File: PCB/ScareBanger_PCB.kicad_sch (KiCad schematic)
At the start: 25 parts, among them J1 RJ45, J16 Conn_01x10_Female - SAINSMART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, J17 Screw_Terminal_01x10 - HILETG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, J2 1757271, J3 Screw_Terminal_01x06, J4 Barrel_Jack_Switch, J5 AudioJack2_Ground, J6 Screw_Terminal_01x06, J7 Screw_Terminal_01x06, J8 Conn_01x04_Female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

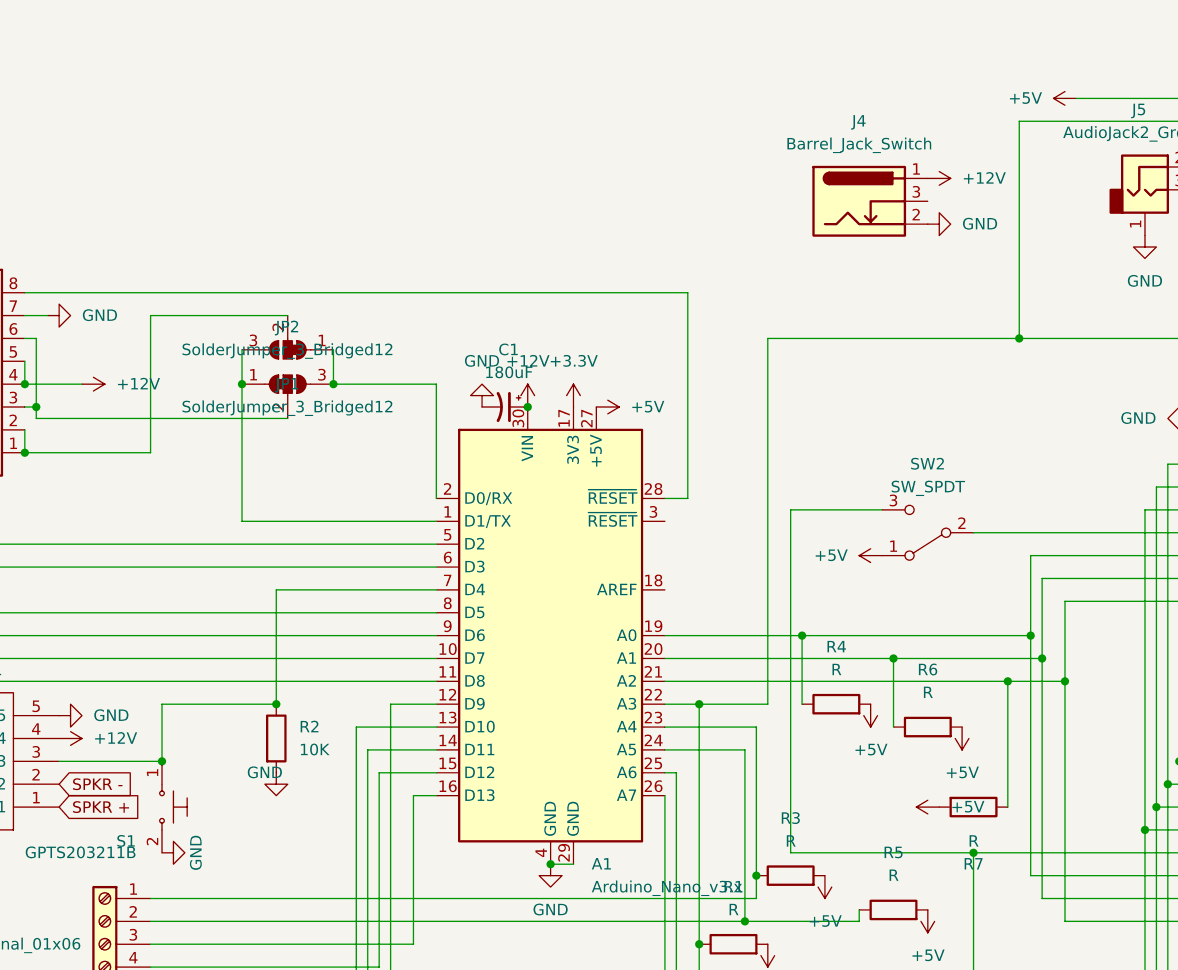
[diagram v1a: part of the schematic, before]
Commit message: added signal cap
added capacitor for signal wire, and  changed the main 12v trace to be 2mm wide
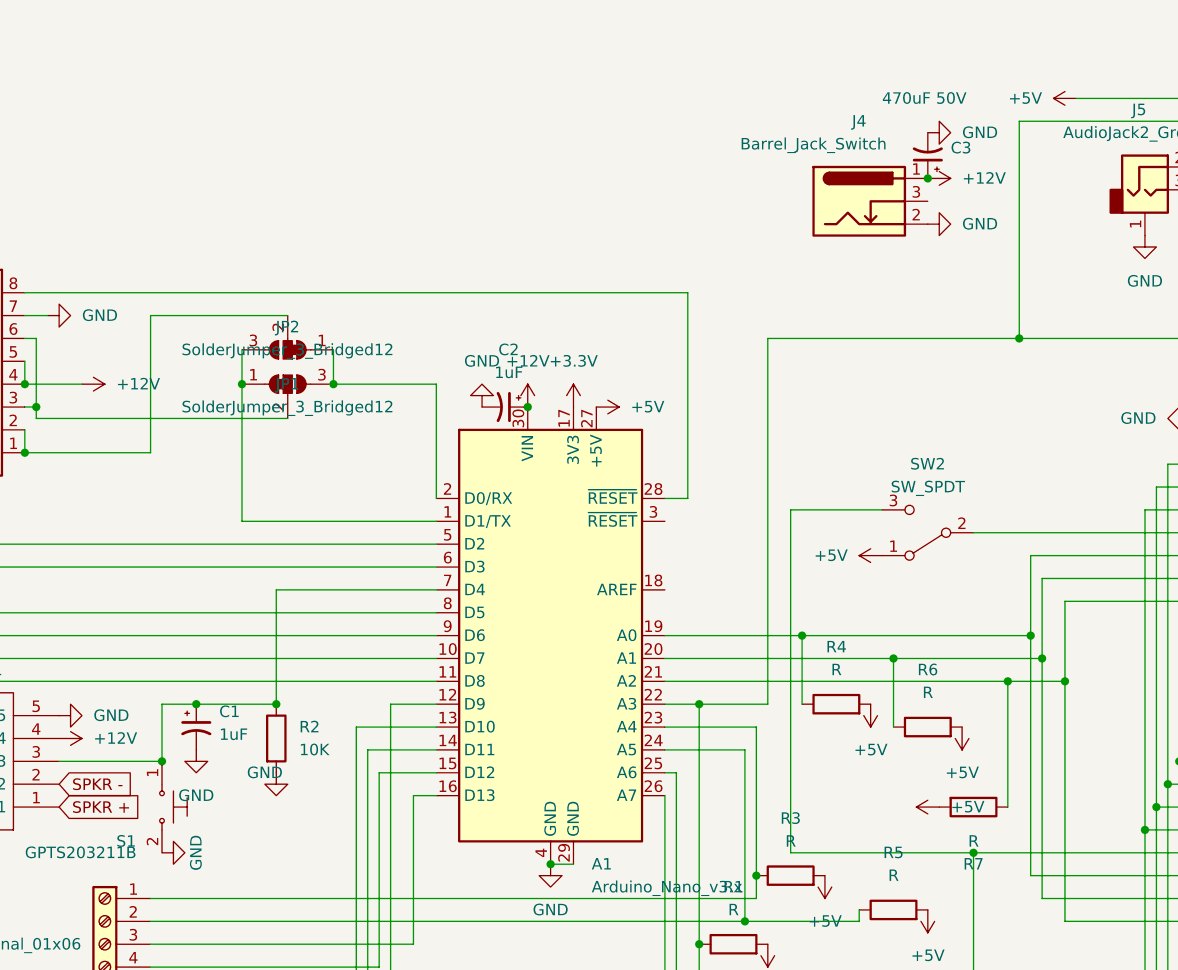
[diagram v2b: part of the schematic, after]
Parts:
- added C2: 1uF, Capacitor_THT:CP_Radial_D4.0mm_P1.50mm, symbol Device:C_Polarized_Small_US
- added C3: 470uF 50V, Capacitor_THT:CP_Radial_D8.0mm_P3.50mm, symbol Device:C_Polarized_Small_US
- C1: value 180uF -> 1uF; footprint Capacitor_THT:CP_Radial_D6.3mm_P2.50mm -> Capacitor_THT:CP_Radial_D4.0mm_P1.50mm
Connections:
- net +12V: now also C2.1, C3.1; no longer C1.1
- net GND: now also C2.2, C3.2
- net at A1.7 (D4), J2.3, R2.1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: now also C1.1
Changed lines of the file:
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@@
   (junction (at 45.72 60.96) (diameter 0) (color 0 0 0 0)
   )
+  (junction (at 144.78 35.56) (diameter 0) (color 0 0 0 0)
+  )
   (junction (at 140.97 88.9) (diameter 0) (color 0 0 0 0)
   )
@@
   (junction (at 168.91 107.95) (diameter 0) (color 0 0 0 0)
   )
+  (junction (at 59.69 100.33) (diameter 0) (color 0 0 0 0)
+  )
+  (junction (at 68.58 58.42) (diameter 0) (color 0 0 0 0)
+  )
+  (junction (at 44.45 58.42) (diameter 0) (color 0 0 0 0)
+  )
+  (junction (at 72.39 93.98) (diameter 0) (color 0 0 0 0)
+  )
+  (junction (at 160.02 91.44) (diameter 0) (color 0 0 0 0)
+  )
+  (junction (at 63.5 93.98) (diameter 0) (color 0 0 0 0)
+  )
+  (junction (at 119.38 93.98) (diameter 0) (color 0 0 0 0)
+  )
+  (junction (at 157.48 88.9) (diameter 0) (color 0 0 0 0)
+  )
+  (junction (at 78.74 58.42) (diameter 0) (color 0 0 0 0)
+  )
+  (junction (at 154.94 53.34) (diameter 0) (color 0 0 0 0)
+  )
+  (junction (at 119.38 120.65) (diameter 0) (color 0 0 0 0)
+  )
+  (junction (at 172.72 100.33) (diameter 0) (color 0 0 0 0)
+  )
   (junction (at 100.33 60.96) (diameter 0) (color 0 0 0 0)
   )
-  (junction (at 59.69 100.33) (diameter 0) (color 0 0 0 0)
-  )
-  (junction (at 68.58 58.42) (diameter 0) (color 0 0 0 0)
-  )
-  (junction (at 44.45 58.42) (diameter 0) (color 0 0 0 0)
-  )
-  (junction (at 72.39 93.98) (diameter 0) (color 0 0 0 0)
-  )
-  (junction (at 160.02 91.44) (diameter 0) (color 0 0 0 0)
-  )
-  (junction (at 119.38 93.98) (diameter 0) (color 0 0 0 0)
-  )
-  (junction (at 157.48 88.9) (diameter 0) (color 0 0 0 0)
-  )
-  (junction (at 78.74 58.42) (diameter 0) (color 0 0 0 0)
-  )
-  (junction (at 154.94 53.34) (diameter 0) (color 0 0 0 0)
-  )
-  (junction (at 119.38 120.65) (diameter 0) (color 0 0 0 0)
-  )
-  (junction (at 172.72 100.33) (diameter 0) (color 0 0 0 0)
-  )
   (junction (at 156.21 86.36) (diameter 0) (color 0 0 0 0)
   )
@@
     (stroke (width 0) (type default) (color 0 0 0 0))
   )
+  (wire (pts (xy 59.69 93.98) (xy 63.5 93.98))
+    (stroke (width 0) (type default) (color 0 0 0 0))
+  )
   (wire (pts (xy 31.75 129.54) (xy 168.91 129.54))
     (stroke (width 0) (type default) (color 0 0 0 0))
@@
     (stroke (width 0) (type default) (color 0 0 0 0))
   )
+  (wire (pts (xy 63.5 93.98) (xy 72.39 93.98))
+    (stroke (width 0) (type default) (color 0 0 0 0))
+  )
   (wire (pts (xy 116.84 101.6) (xy 116.84 140.97))
     (stroke (width 0) (type default) (color 0 0 0 0))
@@
   )
   (wire (pts (xy 83.82 101.6) (xy 90.17 101.6))
-    (stroke (width 0) (type default) (color 0 0 0 0))
-  )
-  (wire (pts (xy 59.69 93.98) (xy 72.39 93.98))
     (stroke (width 0) (type default) (color 0 0 0 0))
   )
@@
     (pin "1")
   )
+  (symbol (lib_id "Device:C_Polarized_Small_US") (at 63.5 96.52 0) (unit 1)
+    (in_bom yes) (on_board yes) (fields_autoplaced)
+    (property "Reference" "C1" (id 0) (at 66.04 94.8181 0)
+      (effects (font (size 1.27 1.27)) (justify left))
+    )
+    (property "Value" "1uF" (id 1) (at 66.04 97.3581 0)
+      (effects (font (size 1.27 1.27)) (justify left))
+    )
+    (property "Footprint" "Capacitor_THT:CP_Radial_D4.0mm_P1.50mm" (id 2) (at 63.5 96.52 0)
+      (effects (font (size 1.27 1.27)) hide)
+    )
+    (property "Datasheet" "~" (id 3) (at 63.5 96.52 0)
+      (effects (font (size 1.27 1.27)) hide)
+    )
+    (pin "1")
+    (pin "2")
+  )
   (symbol (lib_id "power:+3.3V") (at 116.84 173.99 270) (unit 1)
     (in_bom yes) (on_board yes) (fields_autoplaced)
@@
     (pin "1")
   )
+  (symbol (lib_id "power:GND") (at 144.78 30.48 90) (unit 1)
+    (in_bom yes) (on_board yes) (fields_autoplaced)
+    (property "Reference" "#PWR0139" (id 0) (at 151.13 30.48 0)
+      (effects (font (size 1.27 1.27)) hide)
+    )
+    (property "Value" "GND" (id 1) (at 148.59 30.4799 90)
+      (effects (font (size 1.27 1.27)) (justify right))
+    )
+    (property "Footprint" "" (id 2) (at 144.78 30.48 0)
+      (effects (font (size 1.27 1.27)) hide)
+    )
+    (property "Datasheet" "" (id 3) (at 144.78 30.48 0)
+      (effects (font (size 1.27 1.27)) hide)
+    )
+    (pin "1")
+  )
   (symbol (lib_id "Device:R") (at 182.88 26.67 90) (unit 1)
     (in_bom yes) (on_board yes) (fields_autoplaced)
@@
   )
   (symbol (lib_id "power:+12V") (at 144.78 35.56 270) (unit 1)
-    (in_bom yes) (on_board yes) (fields_autoplaced)
+    (in_bom yes) (on_board yes)
     (property "Reference" "#PWR0110" (id 0) (at 140.97 35.56 0)
       (effects (font (size 1.27 1.27)) hide)
     )
-    (property "Value" "+12V" (id 1) (at 148.59 35.5599 90)
+    (property "Value" "+12V" (id 1) (at 148.59 35.56 90)
       (effects (font (size 1.27 1.27)) (justify left))
     )
@@
     (pin "5")
     (pin "6")
+  )
+  (symbol (lib_id "Device:C_Polarized_Small_US") (at 144.78 33.02 180) (unit 1)
+    (in_bom yes) (on_board yes)
+    (property "Reference" "C3" (id 0) (at 147.32 32.1817 0)
+      (effects (font (size 1.27 1.27)) (justify right))
+    )
+    (property "Value" "470uF 50V" (id 1) (at 139.7 26.67 0)
+      (effects (font (size 1.27 1.27)) (justify right))
+    )
+    (property "Footprint" "Capacitor_THT:CP_Radial_D8.0mm_P3.50mm" (id 2) (at 144.78 33.02 0)
+      (effects (font (size 1.27 1.27)) hide)
+    )
+    (property "Datasheet" "~" (id 3) (at 144.78 33.02 0)
+      (effects (font (size 1.27 1.27)) hide)
+    )
+    (pin "1")
+    (pin "2")
   )
   (symbol (lib_id "Connector:Screw_Terminal_01x10") (at 187.96 105.41 0) (unit 1)
@@
     (pin "1")
   )
-  (symbol (lib_id "Device:C_Polarized_Small_US") (at 97.79 60.96 270) (unit 1)
-    (in_bom yes) (on_board yes) (fields_autoplaced)
-    (property "Reference" "C1" (id 0) (at 98.2218 54.61 90))
-    (property "Value" "180uF" (id 1) (at 98.2218 57.15 90))
-    (property "Footprint" "Capacitor_THT:CP_Radial_D6.3mm_P2.50mm" (id 2) (at 97.79 60.96 0)
-      (effects (font (size 1.27 1.27)) hide)
-    )
-    (property "Datasheet" "~" (id 3) (at 97.79 60.96 0)
-      (effects (font (size 1.27 1.27)) hide)
-    )
-    (pin "1")
-    (pin "2")
-  )
   (symbol (lib_id "power:GND") (at 182.88 97.79 270) (unit 1)
     (in_bom yes) (on_board yes) (fields_autoplaced)
@@
     )
     (pin "1")
+  )
+  (symbol (lib_id "Device:C_Polarized_Small_US") (at 97.79 60.96 270) (unit 1)
+    (in_bom yes) (on_board yes) (fields_autoplaced)
+    (property "Reference" "C2" (id 0) (at 98.2218 54.61 90))
+    (property "Value" "1uF" (id 1) (at 98.2218 57.15 90))
+    (property "Footprint" "Capacitor_THT:CP_Radial_D4.0mm_P1.50mm" (id 2) (at 97.79 60.96 0)
+      (effects (font (size 1.27 1.27)) hide)
+    )
+    (property "Datasheet" "~" (id 3) (at 97.79 60.96 0)
+      (effects (font (size 1.27 1.27)) hide)
+    )
+    (pin "1")
+    (pin "2")
   )
   (symbol (lib_id "Device:R") (at 144.78 96.52 90) (unit 1)
@@
   )
   (symbol (lib_id "Connector:Barrel_Jack_Switch") (at 137.16 38.1 0) (unit 1)
-    (in_bom yes) (on_board yes) (fields_autoplaced)
+    (in_bom yes) (on_board yes)
     (property "Reference" "J4" (id 0) (at 137.16 29.21 0))
-    (property "Value" "Barrel_Jack_Switch" (id 1) (at 137.16 31.75 0))
+    (property "Value" "Barrel_Jack_Switch" (id 1) (at 132.08 31.75 0))
     (property "Footprint" "custom:Vertical-BarrelJack_54-00287" (id 2) (at 138.43 39.116 0)
       (effects (font (size 1.27 1.27)) hide)
@@
     (pin "2")
   )
+  (symbol (lib_id "power:GND") (at 63.5 99.06 0) (unit 1)
+    (in_bom yes) (on_board yes) (fields_autoplaced)
+    (property "Reference" "#PWR0138" (id 0) (at 63.5 105.41 0)
+      (effects (font (size 1.27 1.27)) hide)
+    )
+    (property "Value" "GND" (id 1) (at 63.5 104.14 0))
+    (property "Footprint" "" (id 2) (at 63.5 99.06 0)
+      (effects (font (size 1.27 1.27)) hide)
+    )
+    (property "Datasheet" "" (id 3) (at 63.5 99.06 0)
+      (effects (font (size 1.27 1.27)) hide)
+    )
+    (pin "1")
+  )
   (symbol (lib_id "power:GND") (at 144.78 40.64 90) (unit 1)
     (in_bom yes) (on_board yes) (fields_autoplaced)
@@
       (reference "#PWR0137") (unit 1) (value "GND") (footprint "")
     )
+    (path "/f4e3cc6a-3d97-456f-a098-683a69a2cae0"
+      (reference "#PWR0138") (unit 1) (value "GND") (footprint "")
+    )
+    (path "/5bd8d69e-811e-4b0a-9589-b11440f65125"
+      (reference "#PWR0139") (unit 1) (value "GND") (footprint "")
+    )
     (path "/e6cddf47-3ed0-4194-96cf-6e3e8e9dfceb"
       (reference "A1") (unit 1) (value "Arduino_Nano_v3.x") (footprint "SamacSys_Parts:ARDNANO30NP")
     )
-    (path "/a5bbf192-b8fa-493b-abb1-ecb9a27c6f9f"
-      (reference "C1") (unit 1) (value "180uF") (footprint "Capacitor_THT:CP_Radial_D6.3mm_P2.50mm")
+    (path "/35709b65-333f-465d-a221-a0926d3b4c4a"
+      (reference "C1") (unit 1) (value "1uF") (footprint "Capacitor_THT:CP_Radial_D4.0mm_P1.50mm")
+    )
+    (path "/ad2ad6b7-2e48-410d-98b9-6baf0b3060b9"
+      (reference "C2") (unit 1) (value "1uF") (footprint "Capacitor_THT:CP_Radial_D4.0mm_P1.50mm")
+    )
+    (path "/7c59923a-4f4d-4a00-950e-f0af7111f430"
+      (reference "C3") (unit 1) (value "470uF 50V") (footprint "Capacitor_THT:CP_Radial_D8.0mm_P3.50mm")
     )
     (path "/31a8688c-835f-4336-aff9-5d990dfd91f0"
